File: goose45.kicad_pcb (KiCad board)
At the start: 2 copper layers, 248 x 76.4 mm, 180 parts, among them J1 Debugger, J2 USB_C_Receptacle_USB2.0, J3 USART, J4 SPI, Q1 Q_NMOS_GSD, SW1 SW_Push, SW10 SW_Push, SW11 SW_Push, SW12 SW_Push, SW13 SW_Push, SW14 SW_Push, SW15 SW_Push, SW16 SW_Push, SW17 SW_Push, SW18 SW_Push, SW19 SW_Push, SW2 SW_Push, SW20 SW_Push, SW21 SW_Push, SW22 SW_Push, SW23 SW_Push, SW24 SW_Push, SW25 SW_Push, SW26 SW_Push, SW27 SW_Push, SW28 SW_Push, SW29 SW_Push, SW3 SW_Push, SW30 SW_Push, SW31 SW_Push, SW32 SW_Push, SW33 SW_Push, SW34 SW_Push, SW35 SW_Push, SW36 SW_Push, SW37 SW_Push, SW38 SW_Push, SW39 SW_Push, SW4 SW_Push, SW40 SW_Push, SW41 SW_Push, SW42 SW_Push, SW43 SW_Push, SW44 SW_Push, SW45 SW_Push, SW46 SW_Push, SW47 SW_Push, SW48 SW_Push, SW49 SW_Push, SW5 SW_Push, SW50 SW_Push, SW51 SW_Push, SW52 SW_Push, SW53 SW_Push, SW54 SW_Push, SW55 SW_Push, SW56 SW_Push, SW57 SW_Push, SW58 SW_Push, SW59 SW_Push, SW6 SW_Push, SW60 SW_Push, SW61 SW_Push, SW7 SW_Push, SW8 SW_Push, SW9 SW_Push, U1 STM32F103CBTx, U2 USBLC6-2SC6, U3 LM317_SOT-223, X1 Crystal_GND24

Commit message: clean project
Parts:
- removed C1, C2: 22pF/50V, Capacitor_SMD:C_0603_1608Metric
- removed C10, C14: 100nF/16v, Capacitor_SMD:C_0603_1608Metric
- removed C11: 10uF/16v, Capacitor_SMD:C_0805_2012Metric
- removed C12, C8: 100uF/16v, Capacitor_SMD:C_1206_3216Metric
- removed C13, C9: 1uF/16v, Capacitor_SMD:C_0603_1608Metric
- removed C3: 1uF/16V, Capacitor_SMD:C_0603_1608Metric
- removed C4, C5, C6, C7: 100nF/16V, Capacitor_SMD:C_0603_1608Metric
- removed D1, D2, D3: LED, LED_SMD:LED_0805_2012Metric
- removed D10, D11, D12, D13, D14, D15, D16, D17, D18, D19, D20, D21, D22, D23, D24, D25, D26, D27, D28, D29, D30, D31, D32, D33, D34, D35, D36, D37, D38, D39, D4, D40, D41, D42, D43, D44, D45, D46, D47, D48, D49, D5, D50, D51, D52, D6, D7, D8, D9: 1N4148, Diode_SMD:D_0805_2012Metric
- removed H1, H7: MountingHole, MountingHole:MountingHole_3.2mm_M3_Pad
- removed H10, H11, H12, H2, H3, H4, H5, H6, H8, H9: MountingHole, MountingHole:MountingHole_3.2mm_M3_Pad_TopOnly
- removed H13, H14: MountingHole_Pad, NetTie:NetTie-2_SMD_Pad0.5mm
- removed J1: Debugger, Connector_PinHeader_2.00mm:PinHeader_1x05_P2.00mm_Vertical
- removed J2: USB_C_Receptacle_USB2.0, Connector_USB:USB_C_Receptacle_HRO_TYPE-C-31-M-12
- removed J3: USART, Connector_PinHeader_2.00mm:PinHeader_1x03_P2.00mm_Vertical
- removed J4: SPI, Connector_PinHeader_2.00mm:PinHeader_1x05_P2.00mm_Vertical
- removed Q1: Q_NMOS_GSD, Package_TO_SOT_SMD:SOT-23
- removed R1, R10, R11, R12, R13, R14, R16, R17, R26, R3, R5, R6, R7, R8, R9: 10K/5%, Resistor_SMD:R_0603_1608Metric
- removed R15: 330R/5%, Resistor_SMD:R_0603_1608Metric
- removed R18, R19: 5.1K/5%, Resistor_SMD:R_0603_1608Metric
- removed R2, R4: 100K/5%, Resistor_SMD:R_0603_1608Metric
- removed R20, R21, R22: 0R/5%, Resistor_SMD:R_0603_1608Metric
- removed R23, R24: 22R/5%, Resistor_SMD:R_0603_1608Metric
- removed R25: 1.5K/5%, Resistor_SMD:R_0603_1608Metric
- removed R27: 100R/5%, Resistor_SMD:R_0603_1608Metric
- removed R28: 240R/5%, Resistor_SMD:R_0603_1608Metric
- removed R29, R30: 820R/5%, Resistor_SMD:R_0603_1608Metric
- removed SW1, SW2: SW_Push, Button_Switch_SMD:SW_Push_1P1T_NO_CK_KSC6xxJ
- removed SW10, SW11, SW12, SW13, SW14, SW15, SW16, SW17, SW18, SW19, SW20, SW21, SW22, SW23, SW24, SW25, SW26, SW27, SW28, SW29, SW3, SW30, SW31, SW32, SW33, SW34, SW35, SW36, SW37, SW38, SW39, SW4, SW40, SW41, SW42, SW43, SW44, SW45, SW46, SW47, SW48, SW49, SW5, SW50, SW51, SW52, SW53, SW54, SW55, SW56, SW57, SW58, SW59, SW6, SW60, SW61, SW7, SW8, SW9: SW_Push, keyswitches:Kailh_socket_MX
- removed U1: STM32F103CBTx, Package_QFP:LQFP-48_7x7mm_P0.5mm
- removed U2: USBLC6-2SC6, Package_TO_SOT_SMD:SOT-23-6
- removed U3: LM317_SOT-223, Package_TO_SOT_SMD:SOT-223-3_TabPin2
- removed X1: Crystal_GND24, Crystal:Crystal_SMD_TXC_7M-4Pin_3.2x2.5mm
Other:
- board size 248 x 76.4 mm -> 245 x 73.6 mm

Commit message: Update lib and rewrite PCB layout
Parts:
- added C1: 1uF/16V, Capacitor_SMD:C_0603_1608Metric, B.Cu at (61.8, 106.9)
- added C10: 1uF/16V, Capacitor_SMD:C_0603_1608Metric, B.Cu at (61.4, 78.5)
- added C11: 1uF/16V, Capacitor_SMD:C_0603_1608Metric, B.Cu at (74.9, 80.9)
- added C12: 100uF/16V, Capacitor_SMD:C_1206_3216Metric, B.Cu at (59.2, 77.8)
- added C13: 100uF/16V, Capacitor_SMD:C_1206_3216Metric, B.Cu at (71.1, 80.2)
- added C2: 100nF/16V, Capacitor_SMD:C_0603_1608Metric, B.Cu at (53.0, 109.2)
- added C3: 100nF/16V, Capacitor_SMD:C_0603_1608Metric, B.Cu at (49.0, 97.6)
- added C4: 100nF/16V, Capacitor_SMD:C_0603_1608Metric, B.Cu at (61.1, 95.3)
- added C5: 100nF/16V, Capacitor_SMD:C_0603_1608Metric, B.Cu at (65.0, 103.5)
- added C6: 22pF/50V, Capacitor_SMD:C_0603_1608Metric, B.Cu at (58.4, 113.0)
- added C7: 22pF/50V, Capacitor_SMD:C_0603_1608Metric, B.Cu at (54.6, 113.1)
- added C8: 100nF/16V, Capacitor_SMD:C_0603_1608Metric, B.Cu at (73.3, 80.9)
- added C9: 100nF/16V, Capacitor_SMD:C_0603_1608Metric, B.Cu at (63.0, 78.5)
- added D10: 1N4148, Diode_SMD:D_0805_2012Metric, B.Cu at (177.7, 63.5)
- added D11: 1N4148, Diode_SMD:D_0805_2012Metric, B.Cu at (197.0, 63.5)
- added D12: 1N4148, Diode_SMD:D_0805_2012Metric, B.Cu at (216.5, 63.5)
- added D13: 1N4148, Diode_SMD:D_0805_2012Metric, B.Cu at (232.2, 63.5)
- added D14: 1N4148, Diode_SMD:D_0805_2012Metric, B.Cu at (234.9, 63.5)
- added D15: 1N4148, Diode_SMD:D_0805_2012Metric, B.Cu at (34.3, 95.0)
- added D16: 1N4148, Diode_SMD:D_0805_2012Metric, B.Cu at (67.4, 92.9)
- added D17: 1N4148, Diode_SMD:D_0805_2012Metric, B.Cu at (87.5, 92.0)
- added D18: 1N4148, Diode_SMD:D_0805_2012Metric, B.Cu at (106.4, 92.3)
- added D19: 1N4148, Diode_SMD:D_0805_2012Metric, B.Cu at (124.6, 93.5)
- added D2: 1N4148, Diode_SMD:D_0805_2012Metric, B.Cu at (67.5, 81.7)
- added D20: 1N4148, Diode_SMD:D_0805_2012Metric, B.Cu at (126.8, 93.5)
- added D21: 1N4148, Diode_SMD:D_0805_2012Metric, B.Cu at (163.0, 92.0)
- added D22: 1N4148, Diode_SMD:D_0805_2012Metric, B.Cu at (182.4, 92.2)
- added D23: 1N4148, Diode_SMD:D_0805_2012Metric, B.Cu at (201.2, 92.2)
- added D24: 1N4148, Diode_SMD:D_0805_2012Metric, B.Cu at (220.7, 92.0)
- added D25: 1N4148, Diode_SMD:D_0805_2012Metric, B.Cu at (240.8, 92.1)
- added D26: 1N4148, Diode_SMD:D_0805_2012Metric, B.Cu at (263.0, 94.5)
- added D27: 1N4148, Diode_SMD:D_0805_2012Metric, B.Cu at (36.7, 114.1)
- added D28: 1N4148, Diode_SMD:D_0805_2012Metric, B.Cu at (76.5, 113.2)
- added D29: 1N4148, Diode_SMD:D_0805_2012Metric, B.Cu at (79.2, 113.2)
- added D3: 1N4148, Diode_SMD:D_0805_2012Metric, B.Cu at (31.1, 64.4)
- added D30: 1N4148, Diode_SMD:D_0805_2012Metric, B.Cu at (115.1, 111.5)
- added D31: 1N4148, Diode_SMD:D_0805_2012Metric, B.Cu at (130.9, 113.5)
- added D32: 1N4148, Diode_SMD:D_0805_2012Metric, B.Cu at (153.9, 111.0)
- added D33: 1N4148, Diode_SMD:D_0805_2012Metric, B.Cu at (173.1, 111.4)
- added D34: 1N4148, Diode_SMD:D_0805_2012Metric, B.Cu at (191.6, 111.8)
- added D35: 1N4148, Diode_SMD:D_0805_2012Metric, B.Cu at (210.5, 111.8)
- added D36: 1N4148, Diode_SMD:D_0805_2012Metric, B.Cu at (229.8, 111.8)
- added D37: 1N4148, Diode_SMD:D_0805_2012Metric, B.Cu at (243.6, 113.7)
- added D38: 1N4148, Diode_SMD:D_0805_2012Metric, B.Cu at (264.2, 113.6)
- added D39: 1N4148, Diode_SMD:D_0805_2012Metric, B.Cu at (47.6, 129.9)
- added D4: 1N4148, Diode_SMD:D_0805_2012Metric, B.Cu at (63.0, 63.5)
- added D40: 1N4148, Diode_SMD:D_0805_2012Metric, B.Cu at (73.1, 122.2)
- added D41: 1N4148, Diode_SMD:D_0805_2012Metric, B.Cu at (76.5, 122.2)
- added D42: 1N4148, Diode_SMD:D_0805_2012Metric, B.Cu at (129.2, 120.8)
- added D43: 1N4148, Diode_SMD:D_0805_2012Metric, B.Cu at (176.8, 120.8)
- added D44: 1N4148, Diode_SMD:D_0805_2012Metric, B.Cu at (216.3, 122.1)
- added D45: 1N4148, Diode_SMD:D_0805_2012Metric, B.Cu at (243.2, 122.2)
- added D46: 1N4148, Diode_SMD:D_0805_2012Metric, B.Cu at (266.3, 120.8)
- added D48: 1N4148, Diode_SMD:D_0805_2012Metric, B.Cu at (270.6, 77.8)
- added D5: 1N4148, Diode_SMD:D_0805_2012Metric, B.Cu at (65.3, 63.5)
- added D6: 1N4148, Diode_SMD:D_0805_2012Metric, B.Cu at (102.2, 63.5)
- added D7: 1N4148, Diode_SMD:D_0805_2012Metric, B.Cu at (120.8, 63.5)
- added D8: 1N4148, Diode_SMD:D_0805_2012Metric, B.Cu at (123.4, 63.5)
- added D9: 1N4148, Diode_SMD:D_0805_2012Metric, B.Cu at (159.0, 63.5)
- added J1: USB_C_Receptacle_USB2.0, Connector_USB:USB_C_Receptacle_HRO_TYPE-C-31-M-12, B.Cu at (44.9, 60.9)
- added J2: SPI, Connector_PinHeader_2.00mm:PinHeader_1x05_P2.00mm_Vertical, B.Cu at (28.6, 101.9)
- added J3: Conn_01x05_Male, Connector_Molex:Molex_CLIK-Mate_502386-0570_1x05-1MP_P1.25mm_Horizontal, B.Cu at (32.2, 79.7)
- added J4: Debugger, Connector_PinHeader_2.00mm:PinHeader_1x05_P2.00mm_Vertical, B.Cu at (110.5, 76.5)
- added J5: USART, Connector_PinHeader_2.00mm:PinHeader_1x03_P2.00mm_Vertical, B.Cu at (28.6, 94.8)
- added R1: 10K/5%, Resistor_SMD:R_0603_1608Metric, B.Cu at (98.2, 77.2)
- added R10: 10K/5%, Resistor_SMD:R_0603_1608Metric, B.Cu at (68.4, 114.1)
- added R11: 10K/5%, Resistor_SMD:R_0603_1608Metric, B.Cu at (72.4, 114.1)
- added R12: 10K/5%, Resistor_SMD:R_0603_1608Metric, B.Cu at (29.4, 114.2)
- added R13: 10K/5%, Resistor_SMD:R_0603_1608Metric, B.Cu at (47.2, 95.7)
- added R14: 10K/5%, Resistor_SMD:R_0603_1608Metric, B.Cu at (50.1, 95.7)
- added R15: 22R/5%, Resistor_SMD:R_0603_1608Metric, B.Cu at (48.3, 86.6)
- added R16: 5.1K/5%, Resistor_SMD:R_0603_1608Metric, B.Cu at (37.8, 62.1)
- added R17: 5.1K/5%, Resistor_SMD:R_0603_1608Metric, B.Cu at (52.2, 62.1)
- added R18: 22R/5%, Resistor_SMD:R_0603_1608Metric, B.Cu at (50.1, 86.6)
- added R19: 1.5K/5%, Resistor_SMD:R_0603_1608Metric, B.Cu at (52.0, 82.9)
- added R2: 10K/5%, Resistor_SMD:R_0603_1608Metric, B.Cu at (121.5, 76.6)
- added R21: 10K/5%, Resistor_SMD:R_0603_1608Metric, B.Cu at (115.3, 78.9)
- added R22: 10K/5%, Resistor_SMD:R_0603_1608Metric, B.Cu at (111.3, 78.9)
- added R23: 39K/5%, Resistor_SMD:R_0603_1608Metric, B.Cu at (70.4, 76.2)
- added R24: 100R/5%, Resistor_SMD:R_0603_1608Metric, B.Cu at (67.2, 76.2)
- added R25: 10K/5%, Resistor_SMD:R_0603_1608Metric, B.Cu at (64.6, 76.9)
- added R3: 100K/5%, Resistor_SMD:R_0603_1608Metric, B.Cu at (98.2, 75.5)
- added R4: 100K/5%, Resistor_SMD:R_0603_1608Metric, B.Cu at (121.5, 74.4)
- added R5: 10K/5%, Resistor_SMD:R_0603_1608Metric, B.Cu at (29.4, 112.7)
- added R6: 10K/5%, Resistor_SMD:R_0603_1608Metric, B.Cu at (29.4, 115.7)
- added R7: 10K/5%, Resistor_SMD:R_0603_1608Metric, B.Cu at (37.8, 99.5)
- added R8: 10K/5%, Resistor_SMD:R_0603_1608Metric, B.Cu at (37.8, 98.0)
- added R9: 10K/5%, Resistor_SMD:R_0603_1608Metric, B.Cu at (70.4, 114.1)
- added REF**: Stabilizer_Cherry_MX_2.00u, Mounting_Keyboard_Stabilizer.pretty:Stabilizer_Cherry_MX_2.00u, F.Cu at (171.1, 124.1)
- added REF**: Stabilizer_Cherry_MX_2.00u, Mounting_Keyboard_Stabilizer.pretty:Stabilizer_Cherry_MX_2.00u, F.Cu at (123.5, 124.1)
- added SW1: Conn_01x02_Female, Connector_PinHeader_2.00mm:PinHeader_1x02_P2.00mm_Vertical, B.Cu at (101.5, 77.2)
- added SW10: SW_Push, Switch_Keyboard_Hotswap_Kailh.pretty:SW_Hotswap_Kailh_MX, F.Cu at (168.7, 67.0)
- added SW11: SW_Push, Switch_Keyboard_Hotswap_Kailh.pretty:SW_Hotswap_Kailh_MX, F.Cu at (187.8, 67.0)
- added SW12: SW_Push, Switch_Keyboard_Hotswap_Kailh.pretty:SW_Hotswap_Kailh_MX, F.Cu at (206.8, 67.0)
- added SW13: SW_Push, Switch_Keyboard_Hotswap_Kailh.pretty:SW_Hotswap_Kailh_MX, F.Cu at (225.9, 67.0)
- added SW14: SW_Push, Switch_Keyboard_Hotswap_Kailh.pretty:SW_Hotswap_Kailh_MX, F.Cu at (244.9, 67.0)
- added SW15: SW_Push, Switch_Keyboard_Hotswap_Kailh.pretty:SW_Hotswap_Kailh_MX, F.Cu at (37.8, 86.0)
- added SW16: SW_Push, Switch_Keyboard_Hotswap_Kailh.pretty:SW_Hotswap_Kailh_MX, F.Cu at (59.2, 86.0)
- added SW17: SW_Push, Switch_Keyboard_Hotswap_Kailh.pretty:SW_Hotswap_Kailh_MX, F.Cu at (78.2, 86.0)
- added SW18: SW_Push, Switch_Keyboard_Hotswap_Kailh.pretty:SW_Hotswap_Kailh_MX, F.Cu at (97.3, 86.0)
- added SW19: SW_Push, Switch_Keyboard_Hotswap_Kailh.pretty:SW_Hotswap_Kailh_MX, F.Cu at (116.3, 86.0)
- added SW2: SW_Push, Button_Switch_SMD:SW_Push_1P1T_NO_CK_KSC6xxJ, B.Cu at (128.3, 77.9)
- added SW20: SW_Push, Switch_Keyboard_Hotswap_Kailh.pretty:SW_Hotswap_Kailh_MX, F.Cu at (135.4, 86.0)
- added SW21: SW_Push, Switch_Keyboard_Hotswap_Kailh.pretty:SW_Hotswap_Kailh_MX, F.Cu at (154.4, 86.0)
- added SW22: SW_Push, Switch_Keyboard_Hotswap_Kailh.pretty:SW_Hotswap_Kailh_MX, F.Cu at (173.5, 86.0)
- added SW23: SW_Push, Switch_Keyboard_Hotswap_Kailh.pretty:SW_Hotswap_Kailh_MX, F.Cu at (192.5, 86.0)
- added SW24: SW_Push, Switch_Keyboard_Hotswap_Kailh.pretty:SW_Hotswap_Kailh_MX, F.Cu at (211.6, 86.0)
- added SW25: SW_Push, Switch_Keyboard_Hotswap_Kailh.pretty:SW_Hotswap_Kailh_MX, F.Cu at (230.6, 86.0)
- added SW26: SW_Push, Switch_Keyboard_Hotswap_Kailh.pretty:SW_Hotswap_Kailh_MX, F.Cu at (256.8, 86.0)
- added SW27: SW_Push, Switch_Keyboard_Hotswap_Kailh.pretty:SW_Hotswap_Kailh_MX, F.Cu at (42.5, 105.1)
- added SW28: SW_Push, Switch_Keyboard_Hotswap_Kailh.pretty:SW_Hotswap_Kailh_MX, F.Cu at (68.7, 105.1)
- added SW29: SW_Push, Switch_Keyboard_Hotswap_Kailh.pretty:SW_Hotswap_Kailh_MX, F.Cu at (87.8, 105.1)
- added SW3: SW_Push, Switch_Keyboard_Hotswap_Kailh.pretty:SW_Hotswap_Kailh_MX, F.Cu at (35.4, 67.0)
- added SW30: SW_Push, Switch_Keyboard_Hotswap_Kailh.pretty:SW_Hotswap_Kailh_MX, F.Cu at (106.8, 105.1)
- added SW31: SW_Push, Switch_Keyboard_Hotswap_Kailh.pretty:SW_Hotswap_Kailh_MX, F.Cu at (125.9, 105.1)
- added SW32: SW_Push, Switch_Keyboard_Hotswap_Kailh.pretty:SW_Hotswap_Kailh_MX, F.Cu at (144.9, 105.1)
- added SW33: SW_Push, Switch_Keyboard_Hotswap_Kailh.pretty:SW_Hotswap_Kailh_MX, F.Cu at (164.0, 105.1)
- added SW34: SW_Push, Switch_Keyboard_Hotswap_Kailh.pretty:SW_Hotswap_Kailh_MX, F.Cu at (183.0, 105.1)
- added SW35: SW_Push, Switch_Keyboard_Hotswap_Kailh.pretty:SW_Hotswap_Kailh_MX, F.Cu at (202.1, 105.1)
- added SW36: SW_Push, Switch_Keyboard_Hotswap_Kailh.pretty:SW_Hotswap_Kailh_MX, F.Cu at (221.1, 105.1)
- added SW37: SW_Push, Switch_Keyboard_Hotswap_Kailh.pretty:SW_Hotswap_Kailh_MX, F.Cu at (240.2, 105.1)
- added SW38: SW_Push, Switch_Keyboard_Hotswap_Kailh.pretty:SW_Hotswap_Kailh_MX, F.Cu at (261.6, 105.1)
- added SW39: SW_Push, Switch_Keyboard_Hotswap_Kailh.pretty:SW_Hotswap_Kailh_MX, F.Cu at (37.8, 124.1)
- added SW4: SW_Push, Switch_Keyboard_Hotswap_Kailh.pretty:SW_Hotswap_Kailh_MX, F.Cu at (54.4, 67.0)
- added SW40: SW_Push, Switch_Keyboard_Hotswap_Kailh.pretty:SW_Hotswap_Kailh_MX, F.Cu at (61.6, 124.1)
- added SW41: SW_Push, Switch_Keyboard_Hotswap_Kailh.pretty:SW_Hotswap_Kailh_MX, F.Cu at (85.4, 124.1)
- added SW42: SW_Push, Switch_Keyboard_Hotswap_Kailh.pretty:SW_Hotswap_Kailh_MX, F.Cu at (123.5, 124.1)
- added SW43: SW_Push, Switch_Keyboard_Hotswap_Kailh.pretty:SW_Hotswap_Kailh_MX, F.Cu at (171.1, 124.1)
- added SW44: SW_Push, Switch_Keyboard_Hotswap_Kailh.pretty:SW_Hotswap_Kailh_MX, F.Cu at (206.8, 124.1)
- added SW45: SW_Push, Switch_Keyboard_Hotswap_Kailh.pretty:SW_Hotswap_Kailh_MX, F.Cu at (233.0, 124.1)
- added SW46: SW_Push, Switch_Keyboard_Hotswap_Kailh.pretty:SW_Hotswap_Kailh_MX, F.Cu at (259.2, 124.1)
- added SW48: SW_Push, Switch_Keyboard_Hotswap_Kailh.pretty:SW_Hotswap_Kailh_MX, F.Cu at (264.0, 67.0)
- added SW5: SW_Push, Switch_Keyboard_Hotswap_Kailh.pretty:SW_Hotswap_Kailh_MX, F.Cu at (73.5, 67.0)
- added SW6: SW_Push, Switch_Keyboard_Hotswap_Kailh.pretty:SW_Hotswap_Kailh_MX, F.Cu at (92.5, 67.0)
- added SW7: SW_Push, Switch_Keyboard_Hotswap_Kailh.pretty:SW_Hotswap_Kailh_MX, F.Cu at (111.6, 67.0)
- added SW8: SW_Push, Switch_Keyboard_Hotswap_Kailh.pretty:SW_Hotswap_Kailh_MX, F.Cu at (130.6, 67.0)
- added SW9: SW_Push, Switch_Keyboard_Hotswap_Kailh.pretty:SW_Hotswap_Kailh_MX, F.Cu at (149.7, 67.0)
- added U1: STM32F103CBTx, Package_QFP:LQFP-48_7x7mm_P0.5mm, B.Cu at (56.0, 101.5)
- added U2: USBLC6-2SC6, Package_TO_SOT_SMD:SOT-23-6, B.Cu at (43.8, 76.6)
- added U3: TLV75533PDBV, Package_TO_SOT_SMD:SOT-23-5, B.Cu at (67.5, 78.8)
- added X1: Crystal_GND24, Crystal:Crystal_SMD_TXC_7M-4Pin_3.2x2.5mm, B.Cu at (56.7, 110.9)
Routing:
- net GND: track 0.00 -> 295.8 mm, vias 0 -> 11
- net row4: track 0.00 -> 292.5 mm, vias 0 -> 8
- net row2: track 0.00 -> 271.3 mm, vias 0 -> 11
- net row1: track 0.00 -> 269.1 mm, vias 0 -> 4
- net row3: track 0.00 -> 261.2 mm, vias 0 -> 12
- net col12: track 0.00 -> 253.3 mm, vias 0 -> 2
- net col11: track 0.00 -> 243.5 mm, vias 0 -> 2
- net col10: track 0.00 -> 218.7 mm, vias 0 -> 2
- net +3.3V: track 0.00 -> 212.0 mm, vias 0 -> 12
- net col9: track 0.00 -> 193.8 mm, vias 0 -> 2
- net col5: track 0.00 -> 163.1 mm, vias 0 -> 2
- net RESET: track 0.00 -> 155.9 mm, vias 0 -> 2
- net col7: track 0.00 -> 155.7 mm, vias 0 -> 2
- net col8: track 0.00 -> 154.5 mm, vias 0 -> 2
- net col6: track 0.00 -> 126.8 mm, vias 0 -> 2
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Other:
- board size 245 x 73.6 mm -> 247 x 73.6 mm

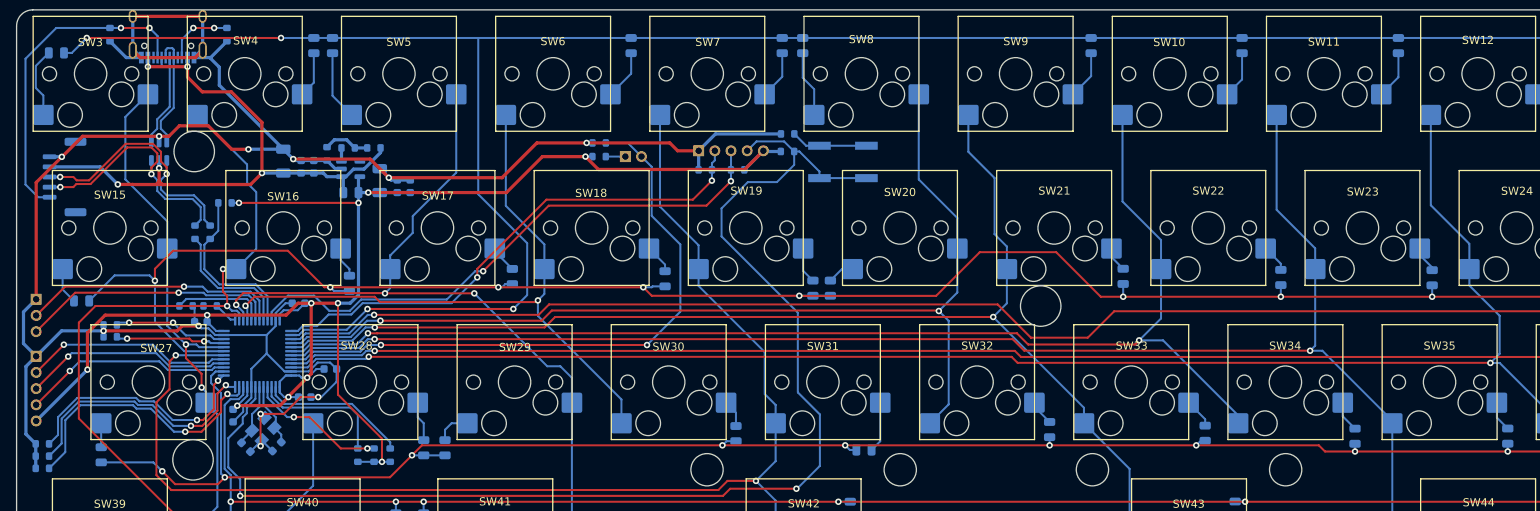
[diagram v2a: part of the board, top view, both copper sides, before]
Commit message: fix PCB GND issue
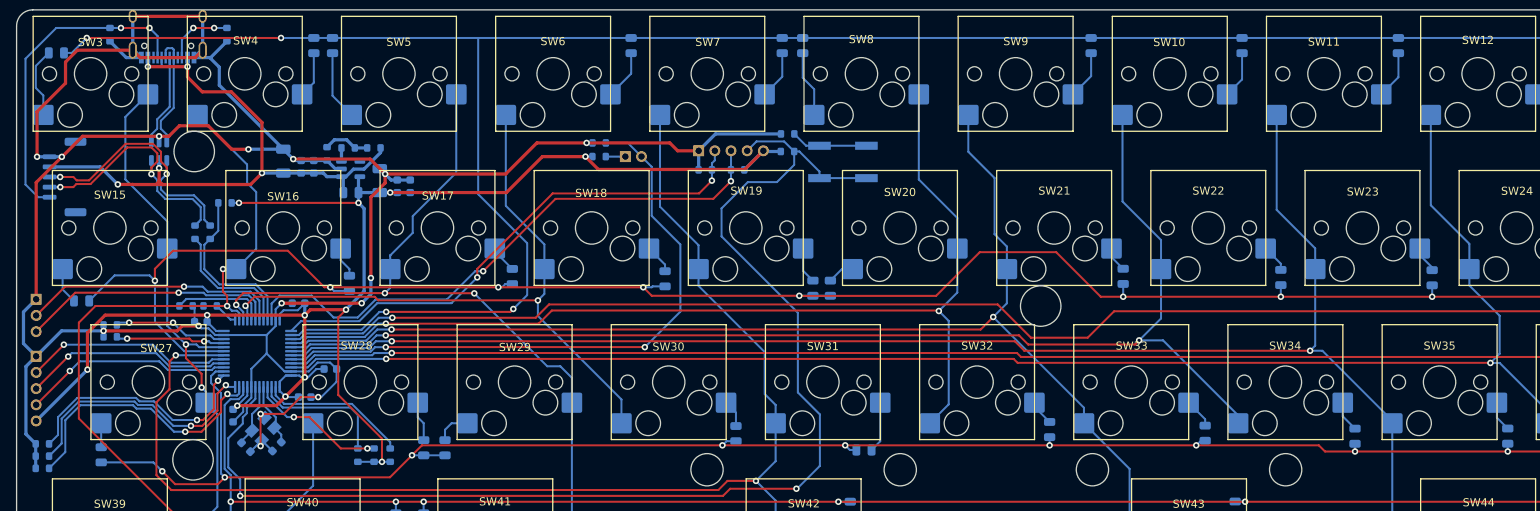
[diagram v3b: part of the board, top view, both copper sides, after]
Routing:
- net GND: track 295.8 -> 346.4 mm, vias 11 -> 15
- net +3.3V: track 212.0 -> 208.1 mm
- net SWDIO: track 69.7 -> 71.0 mm

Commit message: update PCB layout
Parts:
- moved D27 1.04 mm to (37.6, 113.6), turned to 180 degrees
- moved X1 0.80 mm to (56.4, 111.6)
- moved C4 0.64 mm to (61.1, 96.0), turned to 0 degrees
- moved C7 0.60 mm to (54.2, 113.6)
- moved C2 0.28 mm to (53.0, 109.0)
- moved D18 0.23 mm to (106.2, 92.4)
- moved C6 0.08 mm to (58.4, 113.1)
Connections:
- R12 pad 2: PA2 -> PA3
- R5 pad 2: PA3 -> PA4
- R6 pad 2: PA1 -> PA2
- U1 pad 11: PA1 -> row3
- U1 pad 14: row3 -> PA4
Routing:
- net PA1: track 34.2 -> 0.00 mm, vias 2 -> 0
- net PA4: track 0.00 -> 30.0 mm, vias 0 -> 2
- net GND: track 346.4 -> 354.9 mm, vias 15 -> 23
- net col5: track 163.1 -> 158.1 mm
- net +3.3V: track 208.1 -> 204.8 mm, vias 12 -> 13
- net PA2: track 32.2 -> 29.5 mm
- net col2: track 115.1 -> 113.3 mm
- net row3: track 261.2 -> 259.9 mm
- net col8: track 154.3 -> 153.0 mm
- net PA3: track 30.4 -> 29.5 mm
- net MOSI: track 25.7 -> 25.0 mm, vias 1 -> 0
- net XTAL2: track 7.82 -> 8.46 mm
- net VIN: track 76.4 -> 76.9 mm
- net /Interface/CC: track 40.1 -> 39.7 mm, vias 2 -> 3
- net SCK: track 26.0 -> 26.3 mm, vias 1 -> 0
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- added copper zone on B.Cu, net GND
- added copper zone on F.Cu, net GND
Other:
- board text added: "Build your keyboard and enjoy that time."
- board text added: "Design in Taiwan. 2022.10"
- board text added: "Goose45 rev1"

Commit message: add GND via and update PCB height
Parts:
- moved J1 0.35 mm to (44.9, 60.6)
- renumbered REF** to REF1, REF** to REF2
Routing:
- net GND: track 354.9 -> 338.2 mm, vias 23 -> 295
- net col2: track 113.3 -> 114.3 mm
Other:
- board size 247 x 73.6 mm -> 247 x 74.8 mm
